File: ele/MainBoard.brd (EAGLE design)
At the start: 100.1 x 58.3 mm, 55 parts, among them X1 M8, X2 M8, X4 POWER_IN

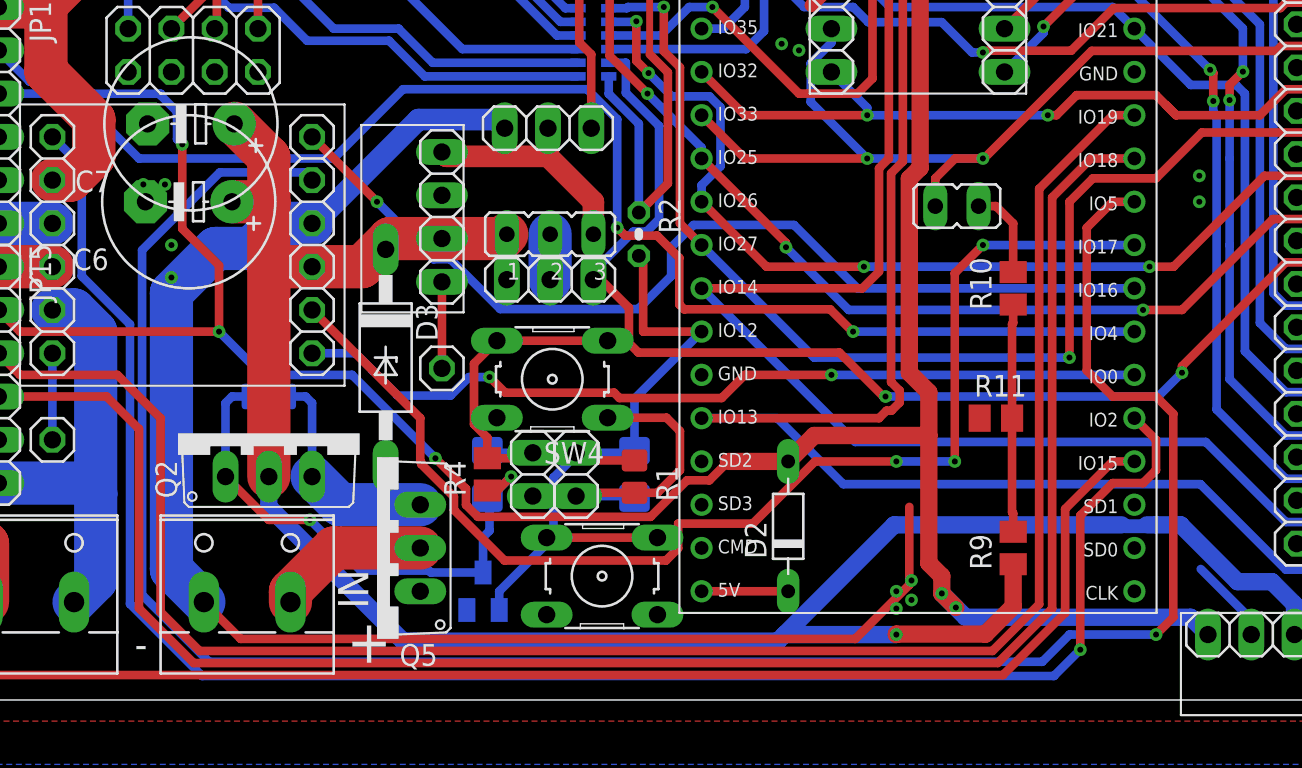
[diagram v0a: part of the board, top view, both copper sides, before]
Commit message: fix_errors
oprava chyb routovani
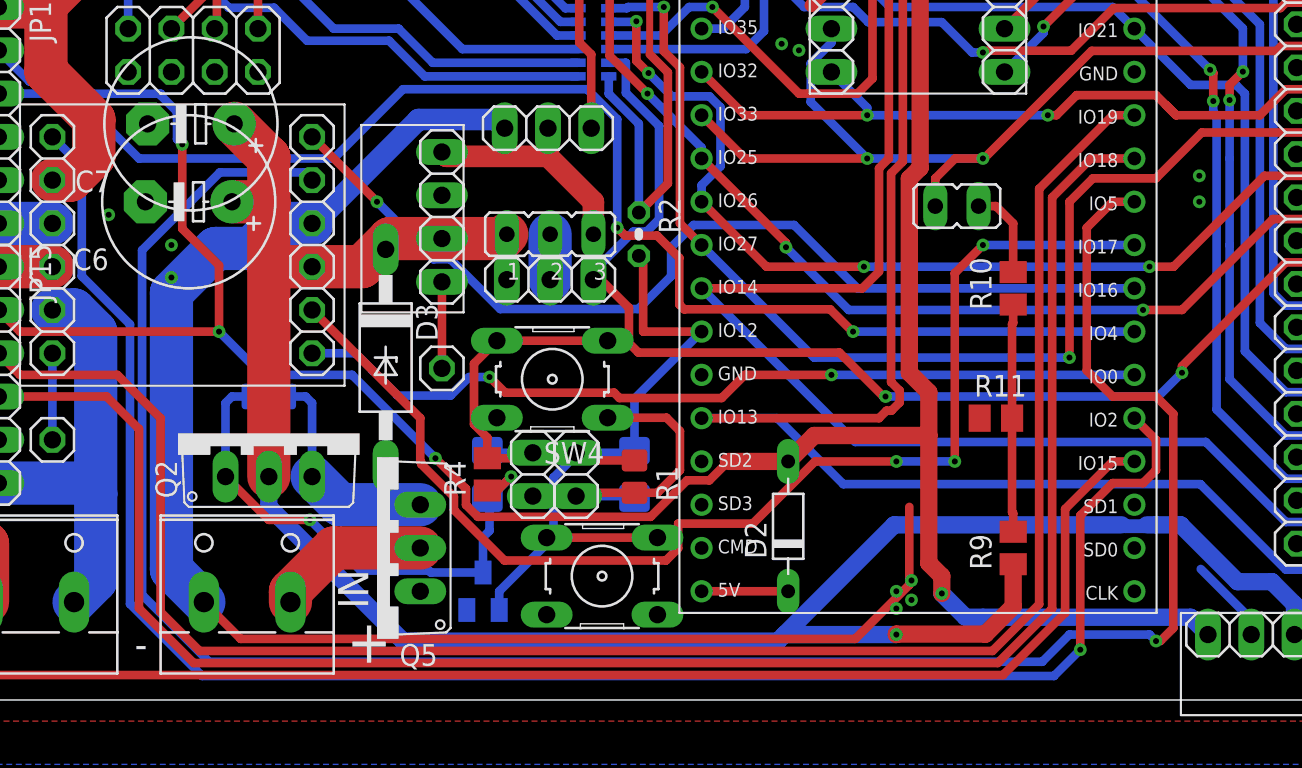
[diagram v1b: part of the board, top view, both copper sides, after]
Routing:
- net VCC: track 130.6 -> 133.4 mm
- net +5V: track 163.7 -> 162.6 mm, vias 5 -> 4
- net PWM2: track 125.4 -> 126.1 mm
- net GND: vias 15 -> 14
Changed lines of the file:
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@@
 <layer number="17" name="Pads" color="2" fill="1" visible="yes" active="yes"/>
 <layer number="18" name="Vias" color="2" fill="1" visible="yes" active="yes"/>
-<layer number="19" name="Unrouted" color="6" fill="1" visible="no" active="yes"/>
+<layer number="19" name="Unrouted" color="6" fill="1" visible="yes" active="yes"/>
 <layer number="20" name="Dimension" color="24" fill="1" visible="no" active="yes"/>
 <layer number="21" name="tPlace" color="7" fill="1" visible="yes" active="yes"/>
@@
 <layer number="46" name="Milling" color="3" fill="1" visible="no" active="yes"/>
 <layer number="47" name="Measures" color="7" fill="1" visible="no" active="yes"/>
-<layer number="48" name="Document" color="7" fill="1" visible="no" active="yes"/>
+<layer number="48" name="Document" color="7" fill="1" visible="yes" active="yes"/>
 <layer number="49" name="Reference" color="7" fill="1" visible="no" active="yes"/>
 <layer number="50" name="dxf" color="7" fill="1" visible="no" active="no"/>
@@
 <text x="26.162" y="0.889" size="2.54" layer="25" font="vector" ratio="20">+</text>
 <text x="13.716" y="1.143" size="1.6764" layer="25" font="vector" ratio="20">-</text>
+<dimension x1="0.508" y1="56.896" x2="0.508" y2="-1.27" x3="-30.48" y3="27.813" textsize="1.016" textratio="20" layer="48"/>
 </plain>
 <attributes>
@@
 </class>
 </classes>
-<designrules name="gatema_2layers *">
+<designrules name="gatema_2layers">
 <description language="de">&lt;b&gt;EAGLE Design Rules&lt;/b&gt;
 &lt;p&gt;
@@
 <wire x1="76.28584375" y1="6.388" x2="79.248" y2="3.42584375" width="0.508" layer="16"/>
 <contactref element="R11" pad="1"/>
-<via x="15.494" y="28.956" extent="1-16" drill="0.35"/>
-<via x="14.224" y="28.956" extent="1-16" drill="0.35"/>
+<via x="12.192" y="27.178" extent="1-16" drill="0.35"/>
 <wire x1="54.61" y1="40.64" x2="53.4384" y2="39.4684" width="0.8128" layer="1"/>
 <via x="1.397" y="24.892" extent="1-16" drill="0.35"/>
@@
 <via x="58.42" y="5.08" extent="1-16" drill="0.35"/>
 <via x="58.42" y="4.064" extent="1-16" drill="0.35"/>
-<wire x1="14.224" y1="28.956" x2="15.494" y2="28.956" width="0" layer="19" extent="1-1"/>
-<wire x1="14.351" y1="27.94" x2="14.224" y2="28.956" width="0" layer="19" extent="1-1"/>
-<wire x1="63.312" y1="15.24" x2="59.182" y2="10.033" width="0" layer="19" extent="1-1"/>
 </signal>
 <signal name="+5V">
@@
 <wire x1="61.087" y1="5.969" x2="60.325" y2="6.731" width="1.016" layer="1"/>
 <via x="61.087" y="4.953" extent="1-16" drill="0.35"/>
-<wire x1="61.9125" y1="4.1275" x2="62.484" y2="3.556" width="1.016" layer="16"/>
 <wire x1="75.692" y1="3.556" x2="76.708" y2="2.54" width="1.016" layer="16"/>
-<wire x1="62.484" y1="3.556" x2="75.692" y2="3.556" width="1.016" layer="16"/>
+<wire x1="63.5" y1="3.556" x2="75.692" y2="3.556" width="1.016" layer="16"/>
 <wire x1="52.07" y1="12.7" x2="48.55695" y2="12.7" width="1.016" layer="1"/>
 <wire x1="48.55695" y1="12.7" x2="47.44895" y2="11.592" width="0.508" layer="1"/>
@@
 <wire x1="58.42" y1="50.546" x2="55.88" y2="50.546" width="1.016" layer="1"/>
 <wire x1="63.5" y1="50.546" x2="62.23" y2="50.546" width="1.016" layer="1"/>
-<via x="61.9125" y="4.1275" extent="1-16" drill="0.35"/>
-<wire x1="61.9125" y1="4.1275" x2="61.087" y2="4.953" width="1.016" layer="16"/>
-<wire x1="61.9125" y1="4.1275" x2="61.087" y2="4.953" width="1.016" layer="1"/>
+<wire x1="63.5" y1="3.556" x2="62.484" y2="3.556" width="1.016" layer="16"/>
+<wire x1="62.484" y1="3.556" x2="61.087" y2="4.953" width="1.016" layer="16"/>
 </signal>
 <signal name="+3V3">
@@
 <signal name="PWM2">
 <contactref element="IM10" pad="IN3"/>
-<via x="73.66" y="2.54" extent="1-16" drill="0.35"/>
-<wire x1="68.58" y1="2.54" x2="73.66" y2="2.54" width="0.508" layer="16"/>
+<via x="73.66" y="2.159" extent="1-16" drill="0.35"/>
 <wire x1="14.151" y1="25.09810625" x2="14.151" y2="4.87389375" width="0.508" layer="16"/>
 <wire x1="18.71689375" y1="29.664" x2="14.151" y2="25.09810625" width="0.508" layer="16"/>
@@
 <wire x1="23.676" y1="29.664" x2="18.71689375" y2="29.664" width="0.508" layer="16"/>
 <wire x1="14.151" y1="4.87389375" x2="18.08189375" y2="0.943" width="0.508" layer="16"/>
-<wire x1="18.08189375" y1="0.943" x2="66.983" y2="0.943" width="0.508" layer="16"/>
-<wire x1="66.983" y1="0.943" x2="68.58" y2="2.54" width="0.508" layer="16"/>
+<wire x1="66.983" y1="0.943" x2="18.08189375" y2="0.943" width="0.508" layer="16"/>
 <contactref element="IM6" pad="29"/>
-<wire x1="73.66" y1="2.54" x2="74.676" y2="3.556" width="0.508" layer="1"/>
-<wire x1="74.676" y1="15.494" x2="74.676" y2="3.556" width="0.508" layer="1"/>
+<wire x1="74.676" y1="2.921" x2="73.914" y2="2.159" width="0.508" layer="1"/>
+<wire x1="73.66" y1="2.159" x2="73.914" y2="2.159" width="0.508" layer="1"/>
+<wire x1="74.676" y1="15.494" x2="74.676" y2="2.921" width="0.508" layer="1"/>
 <wire x1="71.12" y1="27.94" x2="69.596" y2="26.416" width="0.508" layer="1"/>
 <wire x1="69.596" y1="18.034" x2="71.12" y2="16.51" width="0.508" layer="1"/>
@@
 <wire x1="69.596" y1="26.416" x2="69.596" y2="18.034" width="0.508" layer="1"/>
 <wire x1="72.39" y1="27.94" x2="71.12" y2="27.94" width="0.508" layer="1"/>
+<wire x1="73.66" y1="2.159" x2="73.279" y2="2.54" width="0.508" layer="16"/>
+<wire x1="73.279" y1="2.54" x2="68.58" y2="2.54" width="0.508" layer="16"/>
+<wire x1="68.58" y1="2.54" x2="66.983" y2="0.943" width="0.508" layer="16"/>
 </signal>
 <signal name="PWM3">
@@
 <wire x1="51.854" y1="2.54" x2="58.293" y2="8.979" width="1.016" layer="16"/>
 <wire x1="58.42" y1="2.54" x2="51.854" y2="2.54" width="1.016" layer="16"/>
-<wire x1="19.594875" y1="32.548875" x2="19.558" y2="32.512" width="0" layer="19" extent="1-1"/>
+<wire x1="19.558" y1="32.512" x2="21.51625" y2="30.55375" width="2.54" layer="1"/>
+<wire x1="21.51625" y1="30.55375" x2="21.59" y2="30.55375" width="2.54" layer="1"/>
 </signal>
 <signal name="BAT_PROT1">
